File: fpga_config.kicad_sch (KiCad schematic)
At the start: 18 parts, among them J2 Molex 0878321420, U2 XC7A50T-FGG484

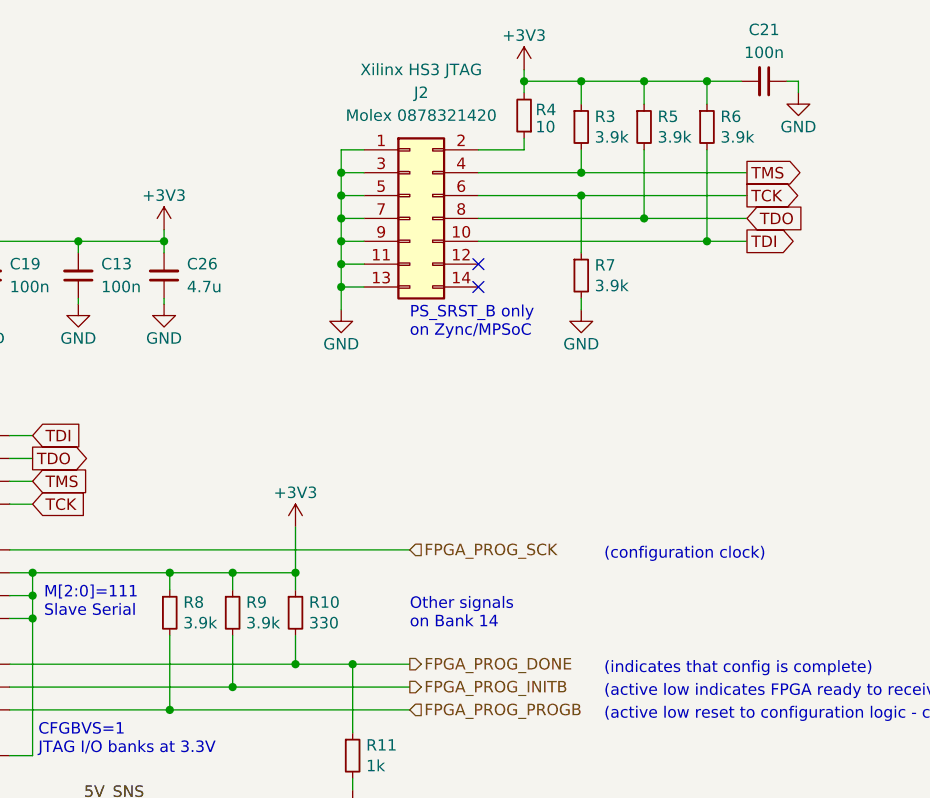
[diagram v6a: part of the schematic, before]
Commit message: Ordered boards from JLCPCB for V1
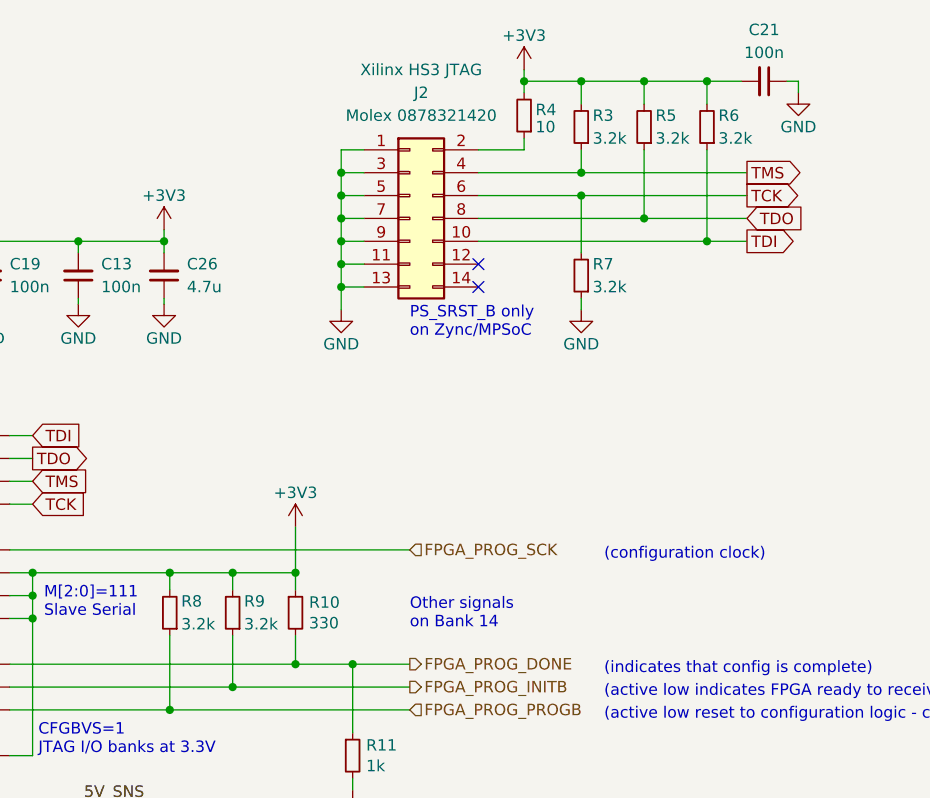
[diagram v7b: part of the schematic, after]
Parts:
- C13, C19, C21, C26: footprint Capacitor_SMD:C_0402_1005Metric_Pad0.74x0.62mm_HandSolder -> Capacitor_SMD:C_0402_1005Metric
- R10: footprint Resistor_SMD:R_0402_1005Metric_Pad0.72x0.64mm_HandSolder -> Resistor_SMD:R_0402_1005Metric; LCSC (none) -> C25104
- R11: footprint Resistor_SMD:R_0402_1005Metric_Pad0.72x0.64mm_HandSolder -> Resistor_SMD:R_0402_1005Metric; LCSC (none) -> C11702
- R3, R5, R6, R7, R8, R9: value 3.9k -> 3.2k; footprint Resistor_SMD:R_0402_1005Metric_Pad0.72x0.64mm_HandSolder -> Resistor_SMD:R_0402_1005Metric; LCSC (none) -> C853935
- R4: footprint Resistor_SMD:R_0402_1005Metric_Pad0.72x0.64mm_HandSolder -> Resistor_SMD:R_0402_1005Metric; LCSC (none) -> C25077
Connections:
- net +3V3: now also R3.2, R5.2, R6.2, R8.2, R9.2; no longer R3.1, R5.1, R6.1, R8.1, R9.1
- net FPGA_PROG_INITB: now also R9.1; no longer R9.2
- net FPGA_PROG_PROGB: now also R8.1; no longer R8.2
- net GND: now also R7.1; no longer R7.2
- net TCK: now also R7.2; no longer R7.1
- net TDI: now also R6.1; no longer R6.2
- net TDO: now also R5.1; no longer R5.2
- net TMS: now also R3.1; no longer R3.2

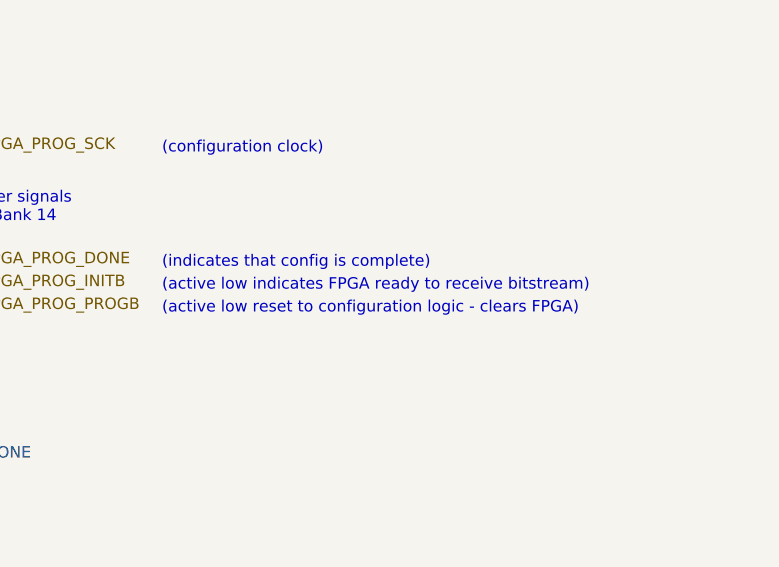
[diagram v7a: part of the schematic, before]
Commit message: Added Python Programming Script
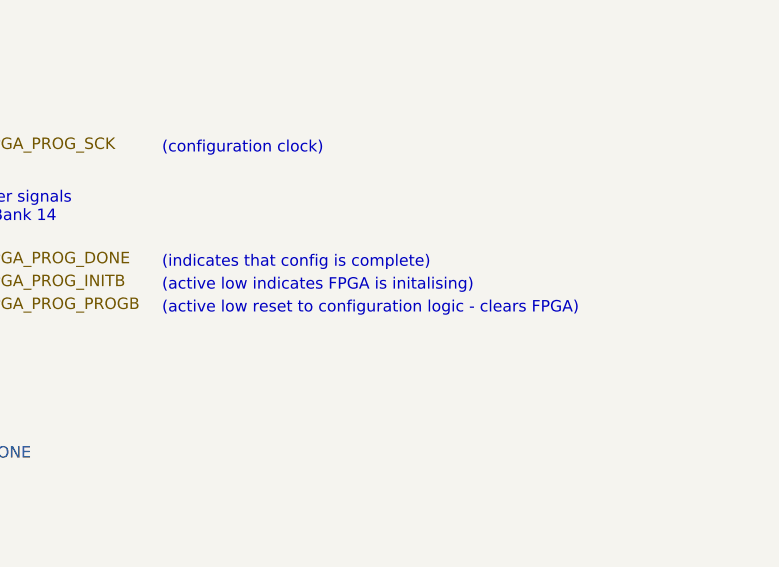
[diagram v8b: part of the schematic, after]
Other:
- note added: "(active low indicates FPGA is initalising)"
- note removed: "(active low indicates FPGA ready to receive bitstream)"
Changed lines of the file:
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@@
     (effects (font (size 1.27 1.27)) (justify left bottom))
   )
-  (text "(active low indicates FPGA ready to receive bitstream)"
-    (at 162.56 99.06 0)
+  (text "(active low indicates FPGA is initalising)" (at 162.56 99.06 0)
     (effects (font (size 1.27 1.27)) (justify left bottom))
   )
